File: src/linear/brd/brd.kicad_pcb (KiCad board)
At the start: 2 copper layers, 100 x 67.8 mm, 93 parts, among them IC1 EFM8BB31F16G-D-QFN24R, J1 out, J2 input, J3 fan, J4 iso_uart, J5 extra, J6 screen, J7 prog, J8 e1, J9 e2, Q1 2N3904, Q2 TIP41C, Q3 2N3904, Q4 TIP41C, U1 TL084h, U2 TL084h, U3 MC33063AD, U4 MC33063AD, U5 LM317, U6 pi121u31

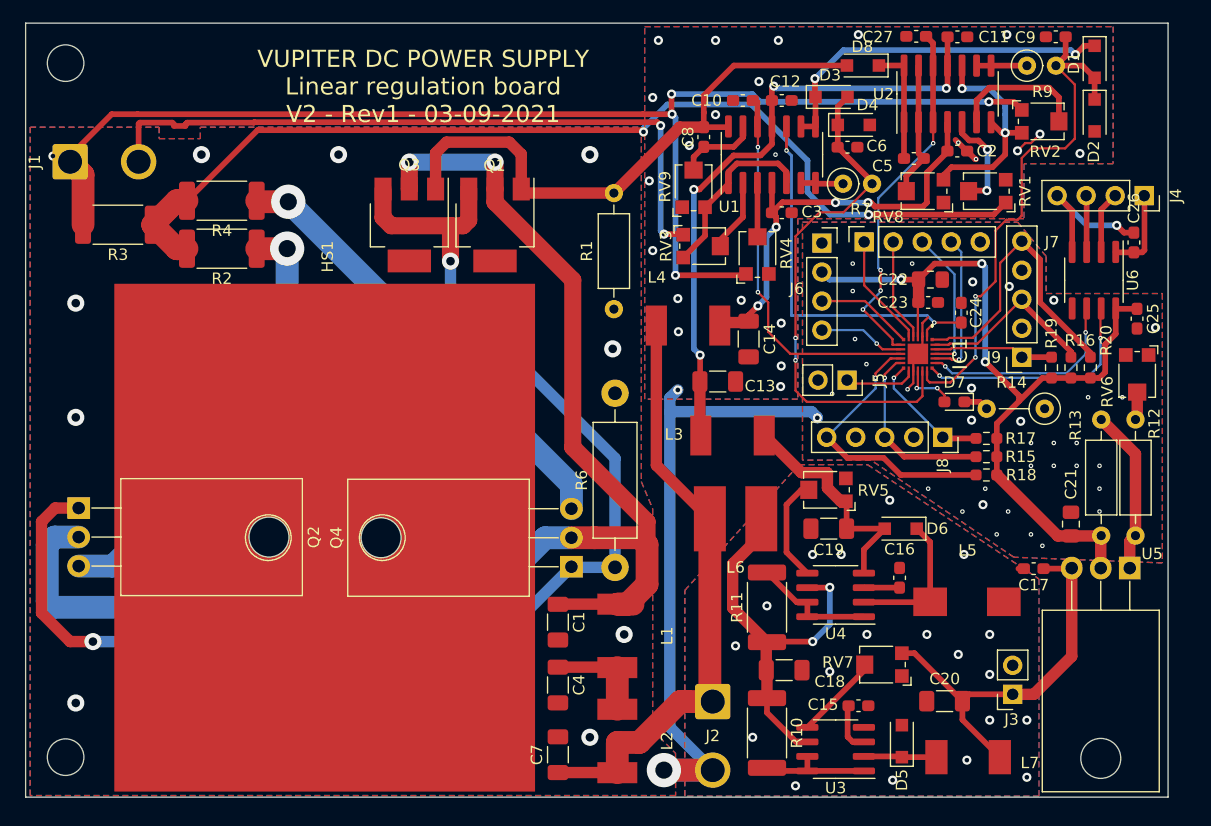
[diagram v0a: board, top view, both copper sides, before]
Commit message: Damped filters on linear stage
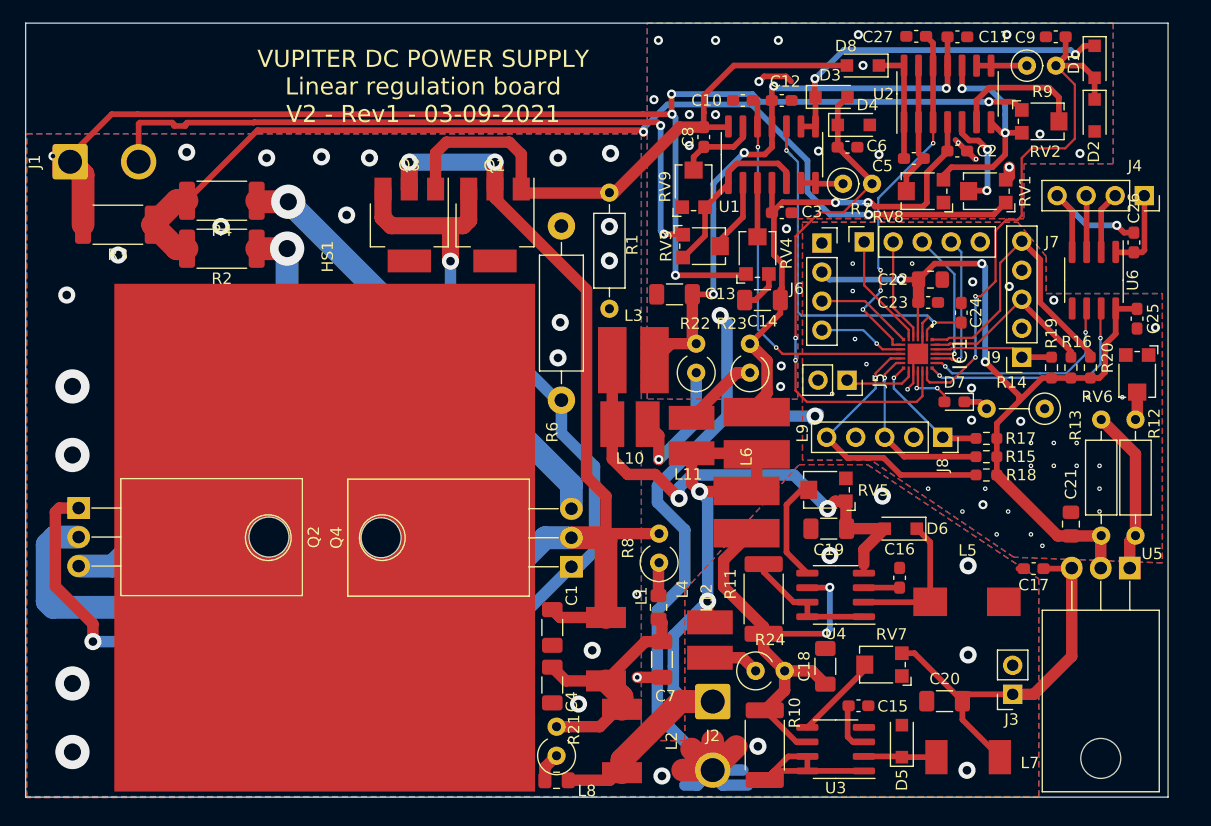
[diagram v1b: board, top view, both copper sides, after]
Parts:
- removed REF** (x2): MountingHole_3.2mm_M3, MountingHole:MountingHole_3.2mm_M3
- added L10: 3.3u, custom:SCCD43, F.Cu at (74.4, 87.6)
- added L11: 3.3u, custom:SCCD43, F.Cu at (79.8, 88.6)
- added L12: 3.3u, custom:SCCD43, F.Cu at (81.4, 106.5)
- added L8: 0.68u, Inductor_SMD:L_0805_2012Metric_Pad1.15x1.40mm_HandSolder, F.Cu at (68.0, 118.8)
- added L9: 6.8u, custom:SCCD54, F.Cu at (85.5, 88.4)
- added R21: 2, Resistor_THT:R_Axial_DIN0309_L9.0mm_D3.2mm_P2.54mm_Vertical, F.Cu at (68.0, 116.6)
- added R22: 2, Resistor_THT:R_Axial_DIN0309_L9.0mm_D3.2mm_P2.54mm_Vertical, F.Cu at (80.2, 83.1)
- added R23: 2, Resistor_THT:R_Axial_DIN0309_L9.0mm_D3.2mm_P2.54mm_Vertical, F.Cu at (84.9, 83.1)
- added R24: 2, Resistor_THT:R_Axial_DIN0309_L9.0mm_D3.2mm_P2.54mm_Vertical, F.Cu at (85.4, 109.2)
- added R8: 2, Resistor_THT:R_Axial_DIN0309_L9.0mm_D3.2mm_P2.54mm_Vertical, F.Cu at (77.0, 99.7)
- L3: value 1.5u -> 6.8u; footprint custom:MCS0630-1R5MN2 -> custom:SCCD54
- L4: value 1.5u -> 0.68u; footprint custom:MCS0630-1R5MN2 -> Inductor_SMD:L_0805_2012Metric_Pad1.15x1.40mm_HandSolder
- L6: value 4.7u -> 6.8u; footprint custom:CR6045-4R7N -> custom:SCCD54
- moved L4 24.8 mm to (76.9, 103.6), turned to 270 degrees
- moved R6 15.4 mm to (68.4, 85.5)
- moved C7 12.3 mm to (77.2, 108.2), turned to 270 degrees
- moved L3 10.9 mm to (74.7, 82.0), turned to 0 degrees
- moved C13 8.52 mm to (78.3, 76.2), turned to 180 degrees
- moved C18 3.62 mm to (91.5, 108.8), turned to 90 degrees
- moved C14 3.62 mm to (86.0, 76.7), turned to 180 degrees
- moved L1 1.53 mm to (72.3, 107.3)
- moved L6 1.12 mm to (84.6, 95.3), turned to 270 degrees
- moved R10 1.08 mm to (86.2, 115.7)
- moved R11 0.79 mm to (86.1, 102.9)
- moved C1 0.68 mm to (67.6, 105.4)
- moved C4 0.49 mm to (67.6, 110.4)
- moved L2 0.41 mm to (73.7, 115.3)
- moved R1 0.39 mm to (72.6, 77.5)
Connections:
- C7 pad 1: vin -> Net-(C4-Pad1)
- L4 pad 1: vin -> Net-(L4-Pad1)
- L4 pad 2: vcc -> Net-(C4-Pad1)
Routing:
- net agp: track 76.2 -> 110.5 mm, vias 86 -> 85
- net pg3: track 21.0 -> 43.9 mm, vias 0 -> 2
- net Net-(C4-Pad1): track 8.87 -> 22.6 mm
- net Net-(L10-Pad2): track 0.00 -> 12.5 mm, vias 0 -> 1
- net Net-(L11-Pad2): track 0.00 -> 6.74 mm
- net vcc: track 38.0 -> 44.7 mm, vias 4 -> 2
- net Net-(Q1-Pad3): track 114.9 -> 108.6 mm
- net Net-(R10-Pad2): track 9.50 -> 14.9 mm
- net vin: track 52.6 -> 57.8 mm, vias 0 -> 2
- net Net-(C18-Pad1): track 35.3 -> 39.8 mm
- net Net-(L12-Pad2): track 0.00 -> 4.48 mm
- net Net-(L4-Pad1): track 0.00 -> 3.39 mm
- net vgg: track 55.3 -> 52.1 mm
- net Net-(L8-Pad2): track 0.00 -> 2.57 mm
- net Net-(R11-Pad2): track 10.8 -> 12.8 mm
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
